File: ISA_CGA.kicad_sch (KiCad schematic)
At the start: 32 parts

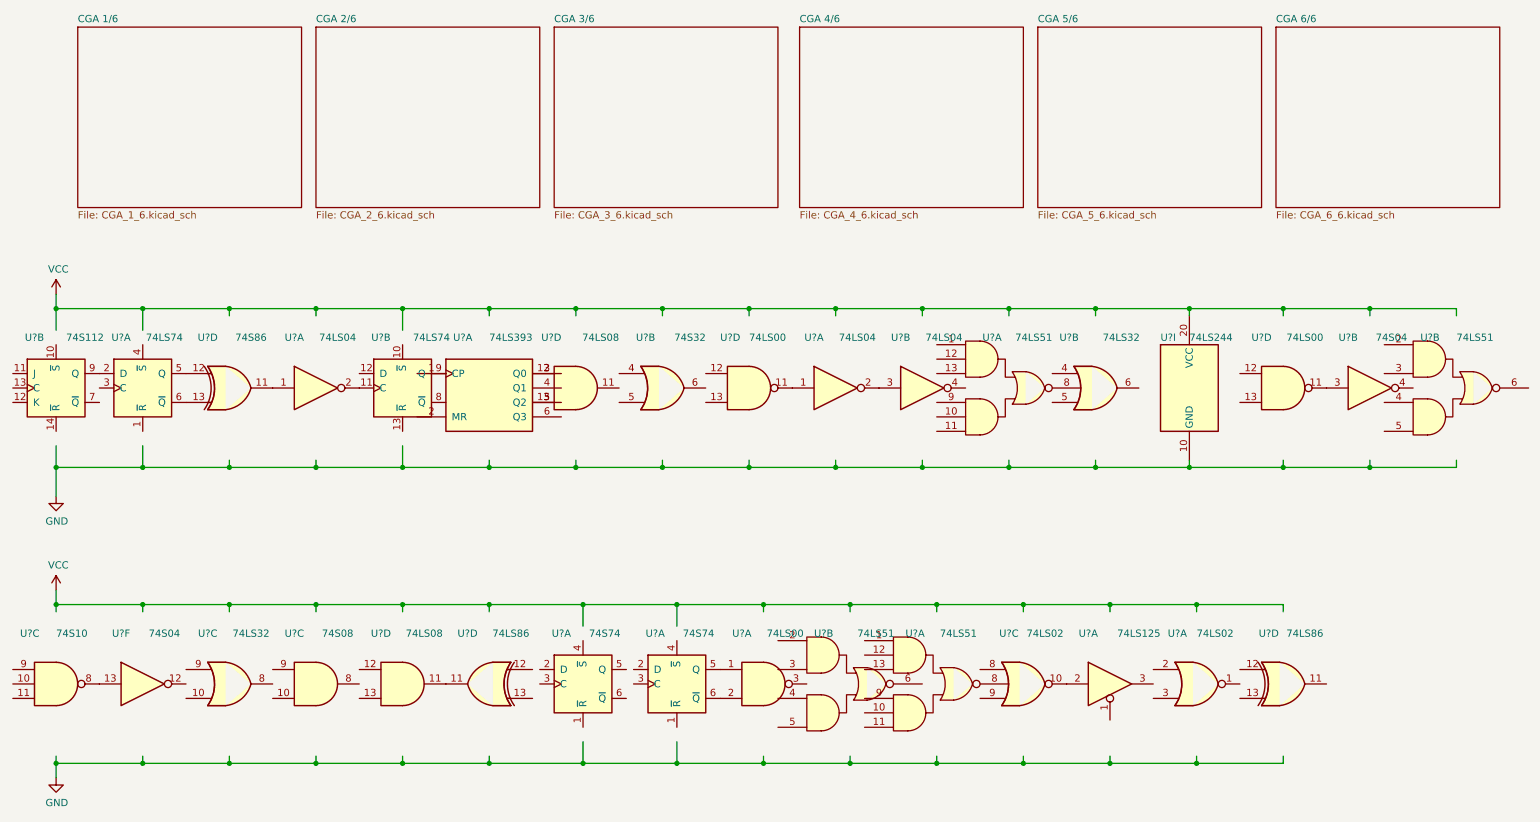
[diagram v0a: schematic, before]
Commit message: Fix Q1' naming thanks to Michael Karcher
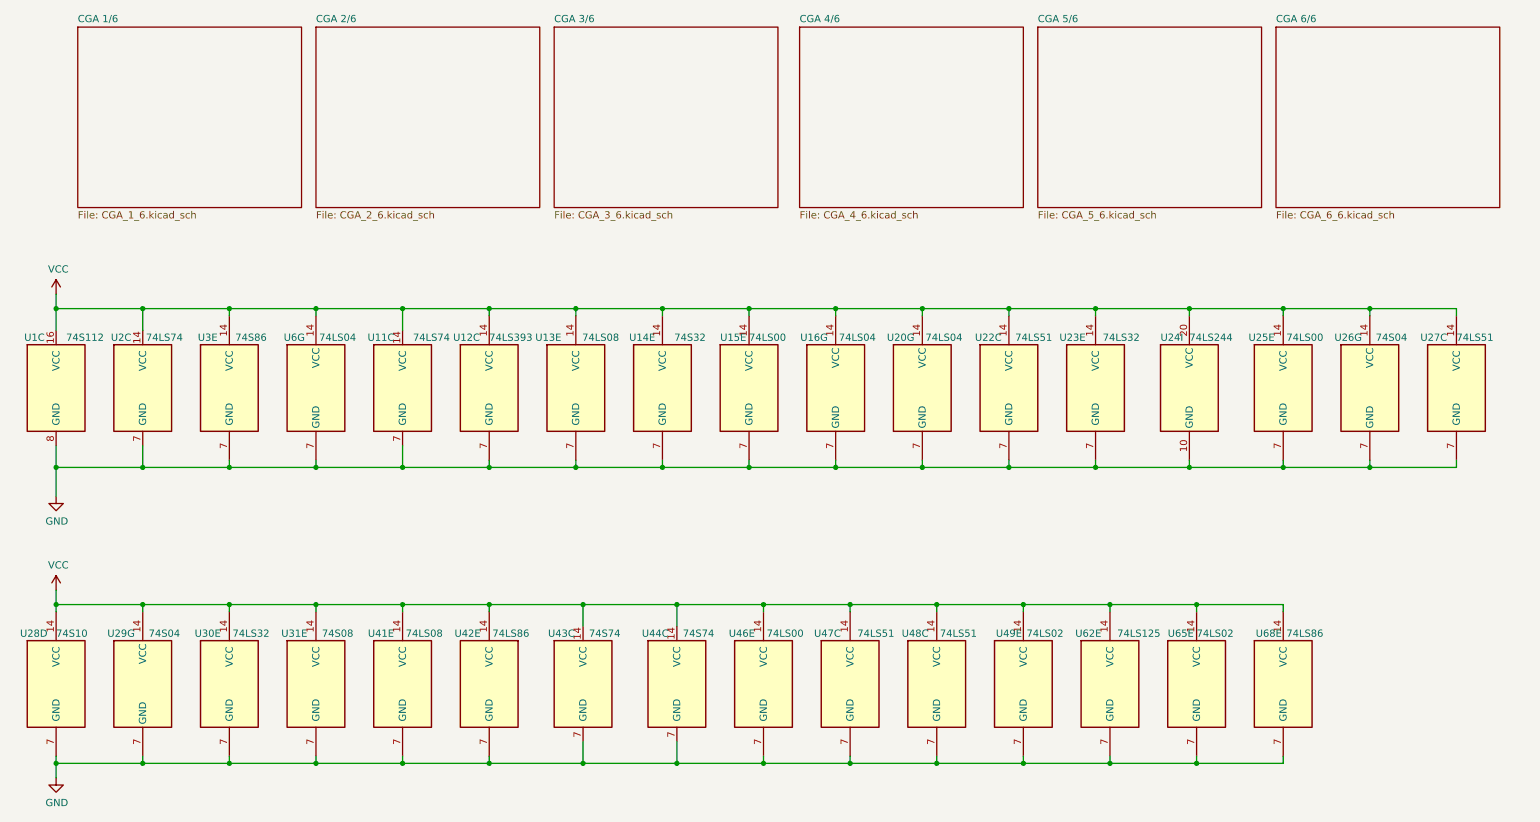
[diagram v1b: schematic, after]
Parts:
- gave numbers to parts that had none: 32
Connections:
- net GND: now also U1.8 (GND), U11.7 (GND), U12.7 (GND), U13.7 (GND), U14.7 (GND), U15.7 (GND), U16.7 (GND), U2.7 (GND), U20.7 (GND), U22.7 (GND), U23.7 (GND), U25.7 (GND), U26.7 (GND), U27.7 (GND), U28.7 (GND), U29.7 (GND), U3.7 (GND), U30.7 (GND), U31.7 (GND), U41.7 (GND), U42.7 (GND), U43.7 (GND), U44.7 (GND), U46.7 (GND), U47.7 (GND), U48.7 (GND), U49.7 (GND), U6.7 (GND), U62.7 (GND), U65.7 (GND), U68.7 (GND)
- net VCC: now also U1.16 (VCC), U11.14 (VCC), U12.14 (VCC), U13.14 (VCC), U14.14 (VCC), U15.14 (VCC), U16.14 (VCC), U2.14 (VCC), U20.14 (VCC), U22.14 (VCC), U23.14 (VCC), U25.14 (VCC), U26.14 (VCC), U27.14 (VCC), U28.14 (VCC), U29.14 (VCC), U3.14 (VCC), U30.14 (VCC), U31.14 (VCC), U41.14 (VCC), U42.14 (VCC), U43.14 (VCC), U44.14 (VCC), U46.14 (VCC), U47.14 (VCC), U48.14 (VCC), U49.14 (VCC), U6.14 (VCC), U62.14 (VCC), U65.14 (VCC), U68.14 (VCC)
